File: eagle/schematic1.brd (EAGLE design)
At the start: 72.4 x 101.6 mm, 32 parts, among them IC1 AD620N, IC2 OP27Z, U7 L7815CV, U8 L7805CV, U9 L7815CV, X1 22-23-2081

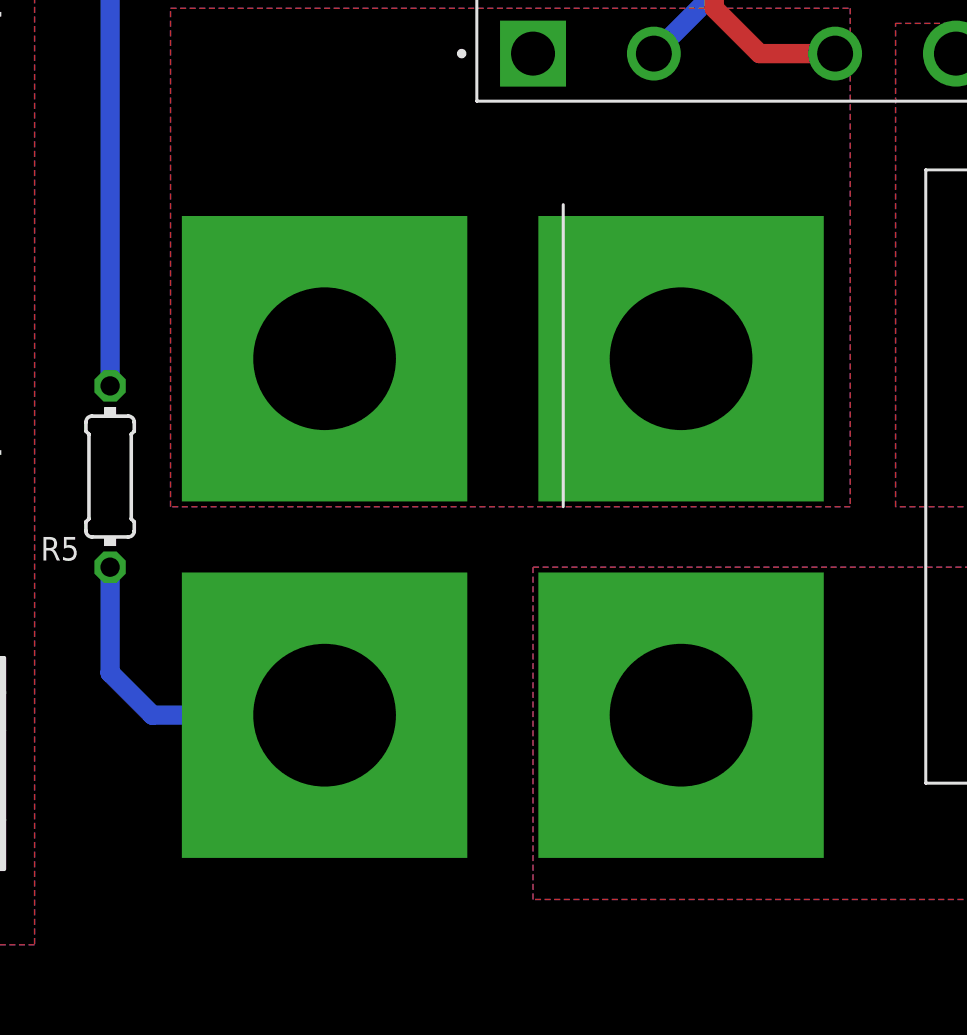
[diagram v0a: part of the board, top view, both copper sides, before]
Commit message: Fixed MOS package - H and V dim are different - Holes are M4 and not M6
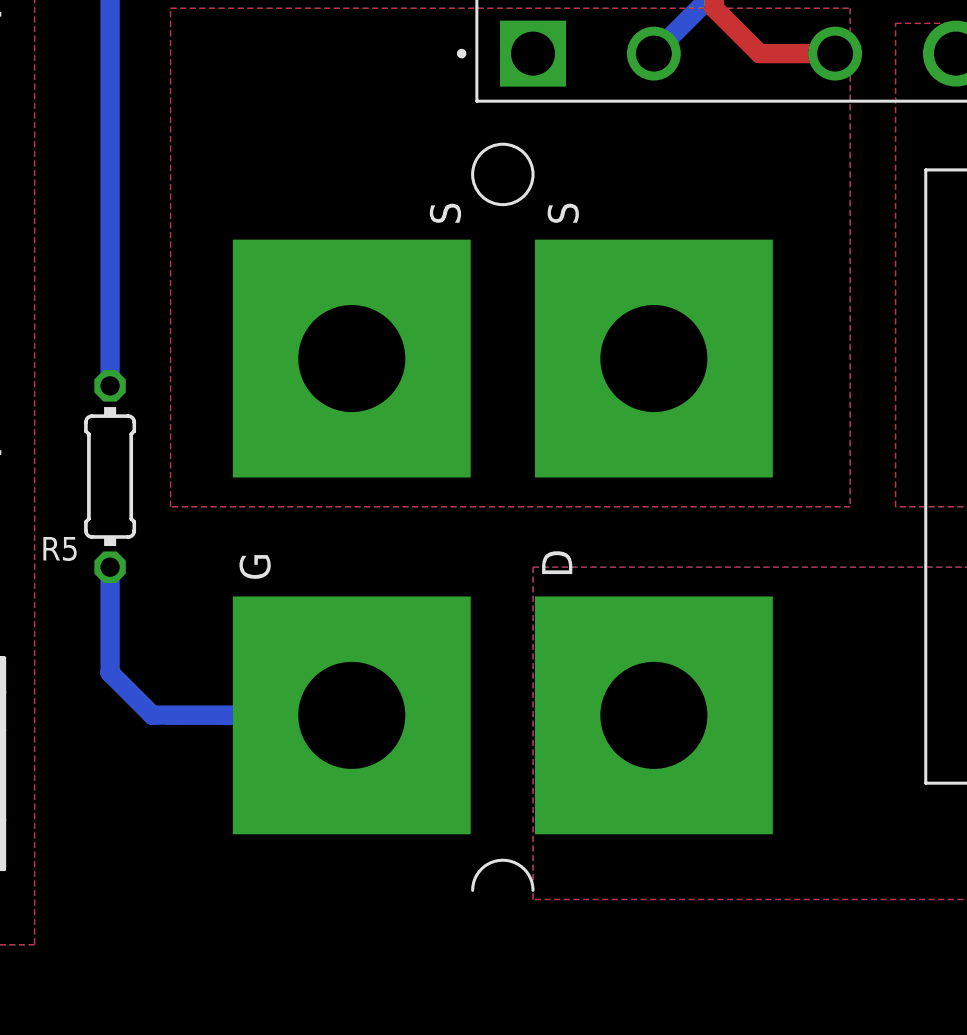
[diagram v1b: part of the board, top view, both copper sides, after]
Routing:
- net N$12: track 14.2 -> 15.3 mm
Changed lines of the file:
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@@
 <wire x1="15.875" y1="24.13" x2="15.875" y2="19.685" width="0.8128" layer="16"/>
 <wire x1="15.875" y1="19.685" x2="17.653" y2="17.907" width="0.8128" layer="16"/>
-<wire x1="17.653" y1="17.907" x2="24.892" y2="17.907" width="0.8128" layer="16"/>
+<wire x1="17.653" y1="17.907" x2="26.035" y2="17.9" width="0.8128" layer="16"/>
 </signal>
 <signal name="3.3V">

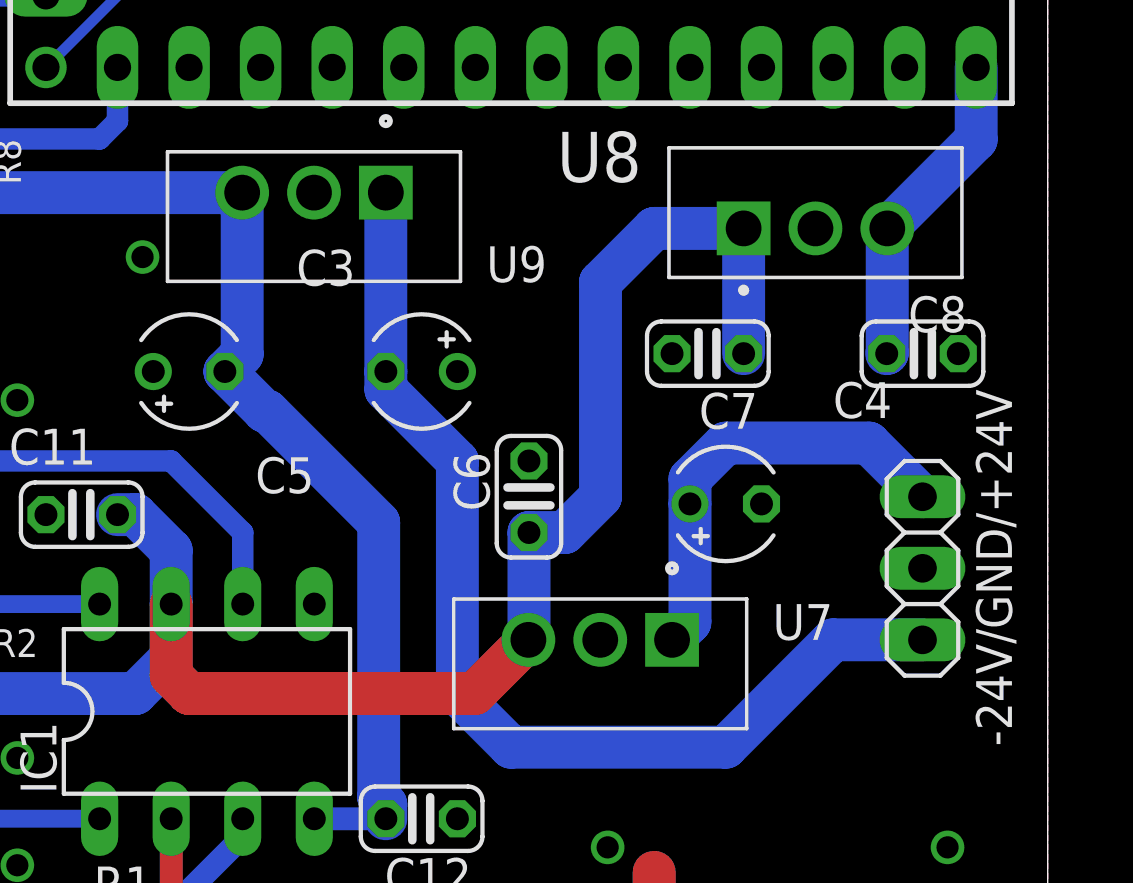
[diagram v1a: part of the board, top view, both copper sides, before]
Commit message: Fixed wrong pinout for negative regulator - This is a classic error that often goes unnoticed. TO2020 Negative regulators have the pinout: 1-GND 2-INPUT 3-OUTPUT This is different from positive regulators with the pinout: 1-INPUT 2-GND 3-OUTPUT Problem fixed. Now the gerbers are ready for production.
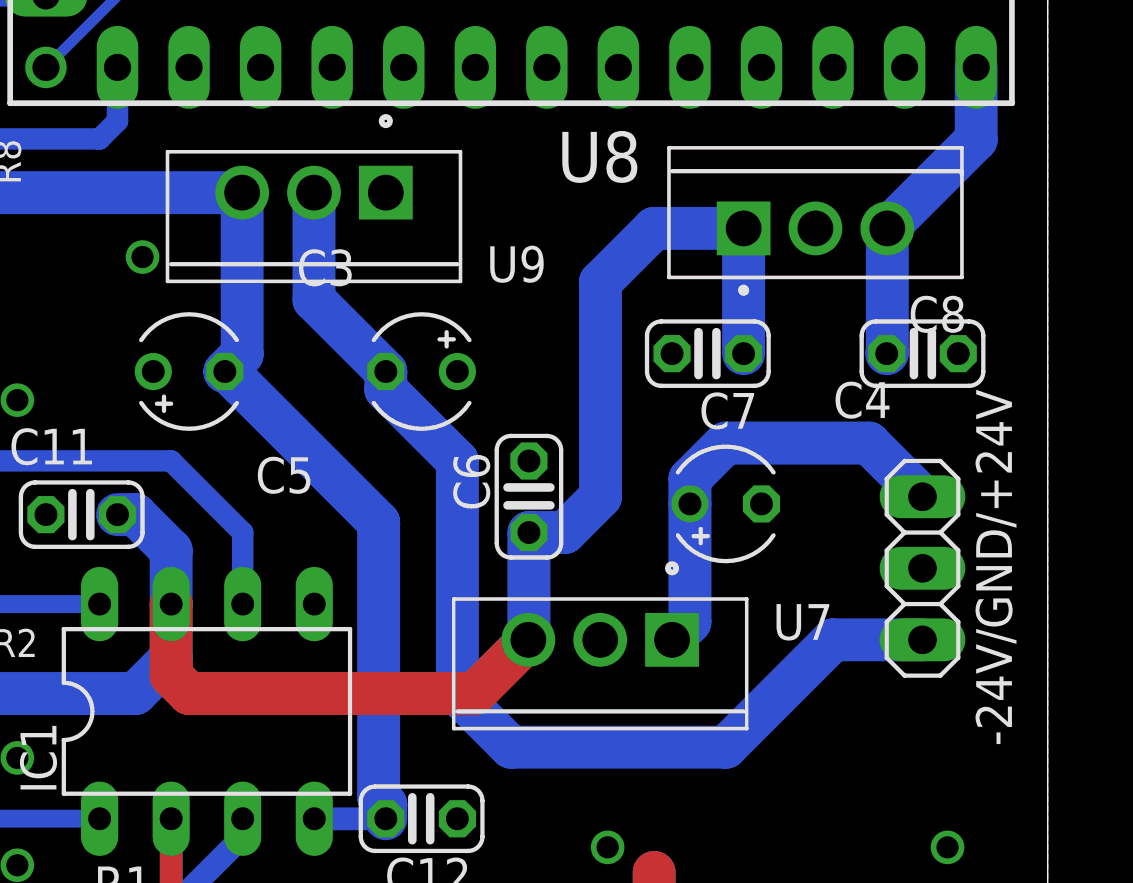
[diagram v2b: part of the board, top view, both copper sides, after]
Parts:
- U9: value L7815CV -> LM7915
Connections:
- net -24V: now also U9.2; no longer U9.1
- net GND: now also U9.1; no longer U9.2
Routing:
- net -24V: track 37.7 -> 38.8 mm
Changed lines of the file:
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@@
 <attribute name="VALUE" x="58.145" y="67.945" size="1.778" layer="27"/>
 </element>
-<element name="U9" library="schematic1" package="TO255P1040X460X1935-3" value="L7815CV" x="48.895" y="73.66" smashed="yes" rot="R180">
-<attribute name="AVAILABILITY" value="Good" x="48.895" y="73.66" size="1.778" layer="27" rot="R180" display="off"/>
-<attribute name="DESCRIPTION" value=" Linear Voltage Regulator IC 1 Output 1.5A TO-220 " x="48.895" y="73.66" size="1.778" layer="27" rot="R180" display="off"/>
-<attribute name="MF" value="STMicroelectronics" x="48.895" y="73.66" size="1.778" layer="27" rot="R180" display="off"/>
-<attribute name="MP" value="L7815CV" x="48.895" y="73.66" size="1.778" layer="27" rot="R180" display="off"/>
+<element name="U9" library="schematic1" package="TO255P1040X460X1935-3" value="LM7915" x="48.895" y="73.66" smashed="yes" rot="R180">
 <attribute name="NAME" x="54.61" y="71.755" size="1.27" layer="25" rot="R180"/>
-<attribute name="PACKAGE" value="TO-220 STMicroelectronics" x="48.895" y="73.66" size="1.778" layer="27" rot="R180" display="off"/>
-<attribute name="PRICE" value="None" x="48.895" y="73.66" size="1.778" layer="27" rot="R180" display="off"/>
-<attribute name="PURCHASE-URL" value="https://pricing.snapeda.com/search/part/L7815CV/?ref=eda" x="48.895" y="73.66" size="1.778" layer="27" rot="R180" display="off"/>
 <attribute name="VALUE" x="51.435" y="78.105" size="1.27" layer="27" rot="R180"/>
 </element>
@@
 <contactref element="U8" pad="2"/>
 <contactref element="C8" pad="2"/>
-<contactref element="U9" pad="2"/>
+<contactref element="U9" pad="1"/>
 <contactref element="U7" pad="2"/>
 <contactref element="IC1" pad="5"/>
@@
 <wire x1="48.895" y1="51.435" x2="48.895" y2="51.943" width="1.524" layer="16"/>
 <wire x1="48.895" y1="51.943" x2="48.641" y2="52.197" width="1.524" layer="16"/>
-<wire x1="44.69500625" y1="65.9003" x2="44.5897" y2="65.9003" width="1.524" layer="16"/>
-<wire x1="44.5897" y1="65.9003" x2="43.18" y2="67.31" width="1.524" layer="16"/>
-<wire x1="48.641" y1="61.95430625" x2="44.69500625" y2="65.9003" width="1.524" layer="16"/>
 <wire x1="48.641" y1="52.197" x2="48.641" y2="61.95430625" width="1.524" layer="16"/>
 <wire x1="43.795" y1="67.925" x2="43.795" y2="73.66" width="1.524" layer="16"/>
+<wire x1="48.641" y1="61.95430625" x2="43.28530625" y2="67.31" width="1.524" layer="16"/>
+<wire x1="43.28530625" y1="67.31" x2="43.18" y2="67.31" width="1.524" layer="16"/>
 </signal>
 <signal name="+24V">
@@
 <signal name="-24V">
 <contactref element="-24V/GND/+24V" pad="3"/>
-<contactref element="U9" pad="1"/>
+<contactref element="U9" pad="2"/>
 <wire x1="67.945" y1="57.785" x2="64.77" y2="57.785" width="1.524" layer="16"/>
 <wire x1="53.34" y1="53.975" x2="51.435" y2="55.88" width="1.524" layer="16"/>
 <wire x1="64.77" y1="57.785" x2="60.96" y2="53.975" width="1.524" layer="16"/>
 <wire x1="60.96" y1="53.975" x2="53.34" y2="53.975" width="1.524" layer="16"/>
-<wire x1="48.895" y1="66.675" x2="51.435" y2="64.135" width="1.524" layer="16"/>
 <wire x1="51.435" y1="55.88" x2="51.435" y2="64.135" width="1.524" layer="16"/>
 <contactref element="C5" pad="-"/>
-<wire x1="48.895" y1="73.66" x2="48.895" y2="67.31" width="1.524" layer="16"/>
-<wire x1="48.895" y1="67.31" x2="48.895" y2="66.675" width="1.524" layer="16"/>
+<wire x1="46.345" y1="73.66" x2="46.345" y2="69.86" width="1.524" layer="16"/>
+<wire x1="51.435" y1="64.135" x2="48.895" y2="66.675" width="1.524" layer="16"/>
+<wire x1="48.895" y1="66.675" x2="48.895" y2="67.31" width="1.524" layer="16"/>
+<wire x1="46.345" y1="69.86" x2="48.895" y2="67.31" width="1.524" layer="16"/>
 </signal>
 <signal name="N$17">

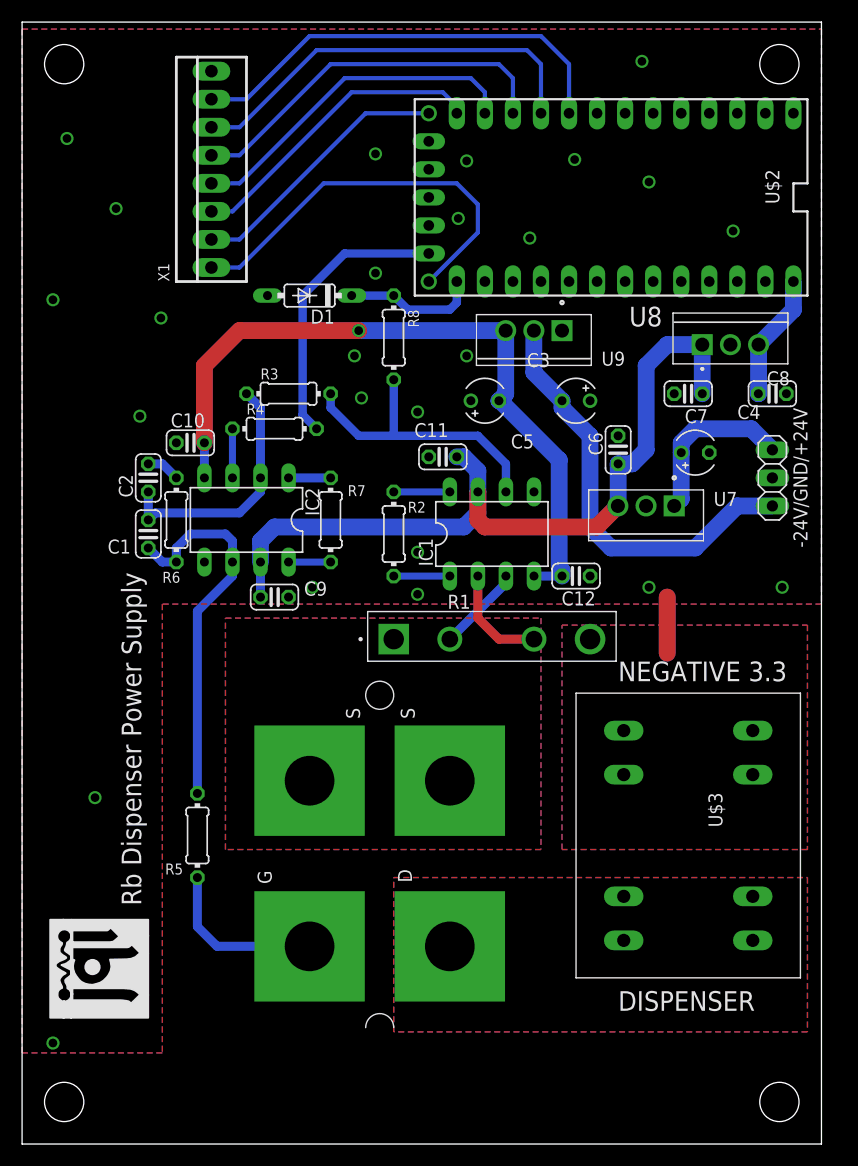
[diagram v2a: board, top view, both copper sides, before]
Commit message: Removed resistor reordered parts and added LPF
- Resistor from pin 1 and 8 of OP27 is a mistake and it was removed.
- Components name re-ordered and re-assigned
- RC filter added after Teensy DAC. It might be necessary to filter
   out digital interference (especially from USB port)
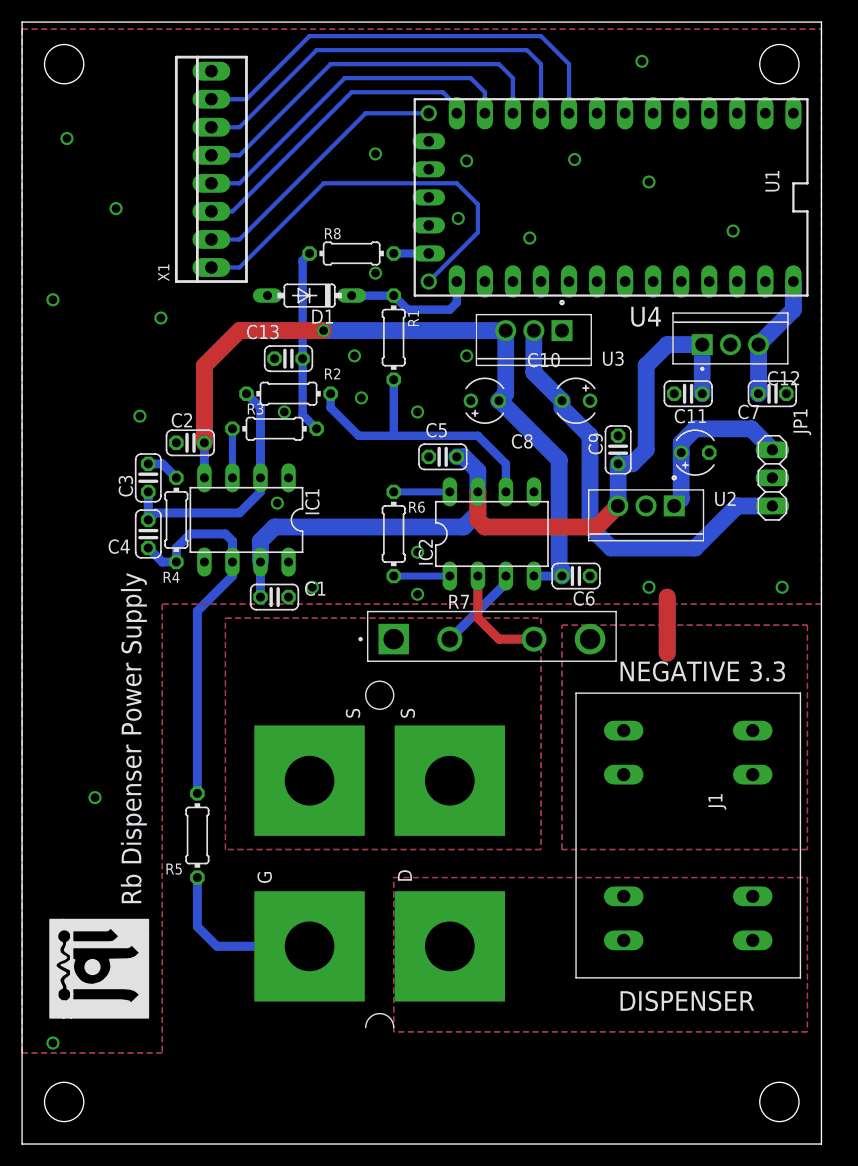
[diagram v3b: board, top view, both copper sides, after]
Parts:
- added C13: (no value), rcl:C025-024X044
- C10, C7, C8: device rcl:C025-024X044 -> rcl:TT2D4
- C3, C4, C5: device rcl:TT2D4 -> rcl:C025-024X044
- IC1: value AD620N -> OP27Z
- IC2: value OP27Z -> AD620N
- R1: value FHR4V-0R1F1 -> (none); device schematic1:RIEDON_FHR4V-0R1F1 -> rcl:0204/7
- R7: value (none) -> FHR4V-0R1F1; device rcl:0204/7 -> schematic1:RIEDON_FHR4V-0R1F1
- moved C4 50.1 mm to (11.4, 55.2), turned to 270 degrees
- moved C9 33.9 mm to (54.0, 62.9), turned to 90 degrees
- moved C3 31.3 mm to (11.4, 60.3), turned to 90 degrees
- moved R1 28.7 mm to (33.7, 73.0), turned to 270 degrees
- moved C10 26.9 mm to (41.9, 67.3)
- moved C12 24.3 mm to (67.9, 67.9), turned to 0 degrees
- moved C11 22.9 mm to (60.3, 67.9)
- moved IC1 22.3 mm to (20.3, 56.5), turned to 180 degrees
- moved IC2 22.3 mm to (42.5, 55.2), turned to 0 degrees
- moved R6 19.7 mm to (33.7, 55.2)
- moved R7 18.2 mm to (42.5, 45.7), turned to 0 degrees
- moved C8 17.8 mm to (50.2, 67.3), turned to 180 degrees
- moved R2 15.9 mm to (24.1, 67.9), turned to 0 degrees
- moved C5 13.1 mm to (38.1, 62.2)
- moved C1 12.8 mm to (22.9, 49.5), turned to 0 degrees
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- renumbered -24V/GND/+24V to JP1, U$1 to T1, U$2 to U1, U$3 to J1, U7 to U2, U8 to U4, U9 to U3
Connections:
- net +15V: now also C1.1, C5.1; no longer C6.1, C7.1
- net +24V: now also C7.+; no longer C4.+
- net +5V: now also C12.1; no longer C8.1
- net -15V: now also C10.-, C2.2, C6.2; no longer C10.2, C12.2, C3.-
- net -24V: now also C8.-; no longer C5.-
- net GND: now also C1.2, C10.+, C12.2, C13.2, C2.1, C5.2, C6.1, C7.-, C8.+, IC2.5, R7.4; no longer C10.1, C12.1, C3.+, C4.-, C5.+, C6.2, C7.2, C8.2, IC1.5, R1.4
- net N$10: now also R8.2; no longer R4.2
- net N$11: now also C4.2, IC1.6, R4.2; no longer C1.2, IC2.6, R6.2
- net N$13: now also C3.2, R4.1; no longer C2.2, R6.1
- net N$14: now also C13.1, R3.2, R8.1; no longer IC2.1, R7.2
- net N$15: now also IC1.8; no longer IC2.8, R7.1
- net N$17: now also R7.1; no longer R1.1
- net N$18: now also IC2.3, R7.2; no longer IC1.3, R1.2
- net N$19: now also IC2.2, R7.3; no longer IC1.2, R1.3
- net N$3: now also R1.1; no longer R8.1
- net N$4: now also IC2.1, R6.2; no longer IC1.1, R2.2
- net N$5: now also IC2.8, R6.1; no longer IC1.8, R2.1
- net N$7: now also IC2.6, R1.2, R2.2; no longer IC1.6, R3.2, R8.2
- net N$8: now also C3.1, C4.1, IC1.2, R2.1; no longer C1.1, C2.1, IC2.2, R3.1
- net N$9: now also IC1.3, R3.1; no longer IC2.3, R4.1
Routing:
- net N$10: track 25.6 -> 3.17 mm
- net N$14: track 3.81 -> 16.7 mm
- net N$15: track 3.81 -> 0.00 mm
- net GND: vias 25 -> 27

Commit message: Changed value of sensing resistor to 0.01Ohm and added value for R6 TO DO:   1 - Add missing values for resistors and capacitors according with the prototype board   2 - Fix the hole size  for the large   3 - Update gerber zip file to reflect change in hole size.
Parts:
- R6: value (none) -> 7.2k
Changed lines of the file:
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@@
 <attribute name="VALUE" x="23.876" y="57.15" size="1.27" layer="27" ratio="10" rot="R180"/>
 </element>
-<element name="R6" library="rcl" library_urn="urn:adsk.eagle:library:334" package="0204/7" package3d_urn="urn:adsk.eagle:package:23498/2" value="" x="33.655" y="55.245" smashed="yes" rot="R270">
+<element name="R6" library="rcl" library_urn="urn:adsk.eagle:library:334" package="0204/7" package3d_urn="urn:adsk.eagle:package:23498/2" value="7.2k" x="33.655" y="55.245" smashed="yes" rot="R270">
 <attribute name="NAME" x="34.925" y="57.1754" size="0.9906" layer="25" ratio="10"/>
 <attribute name="POPULARITY" value="48" x="-50.165" y="22.225" size="1.778" layer="27" rot="R270" display="off"/>
